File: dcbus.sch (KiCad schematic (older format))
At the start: 15 parts, among them K1 CONN_3, T1 COMMON MODE CHOKE

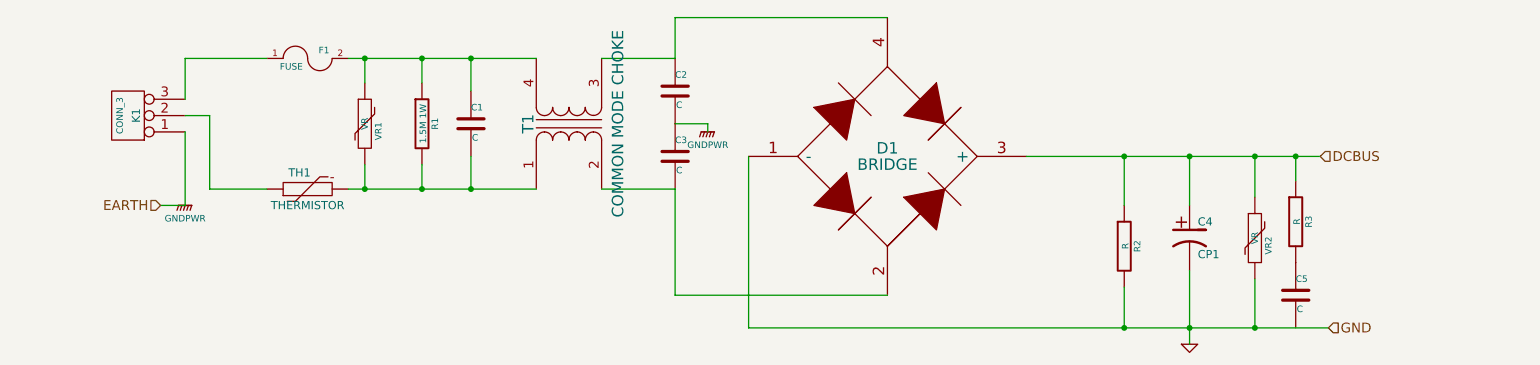
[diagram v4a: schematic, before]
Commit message: Add more protection, MOV to earth, MOV on dcbus
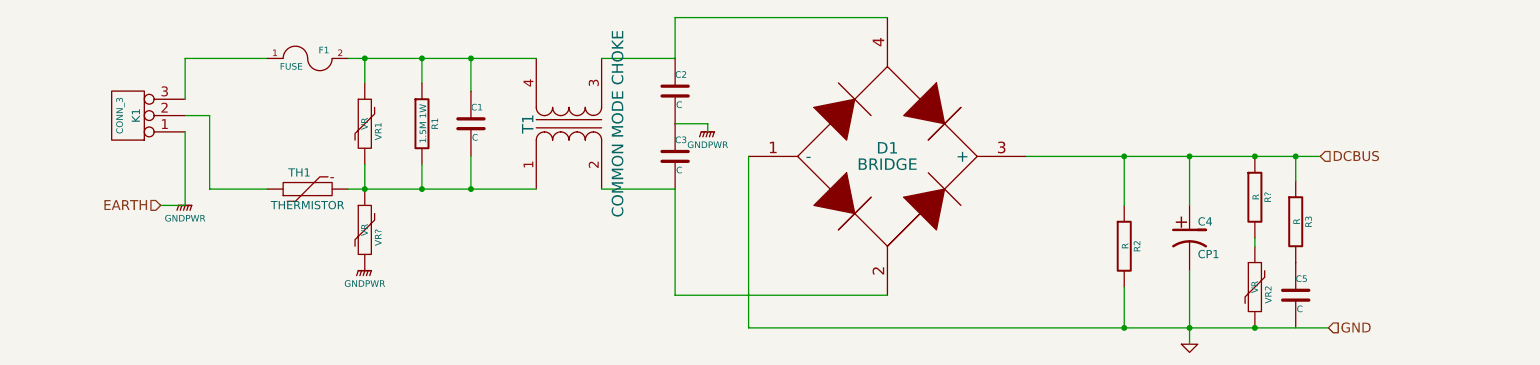
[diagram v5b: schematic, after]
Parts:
- added R?: R, symbol R
- added VR?: VR, symbol VR
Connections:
- net DCBUS: now also R?.1; no longer VR2.1
- net GNDPWR: now also VR?.2
- net at C1.2, R1.2, T1.1 (AA)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: now also VR?.1
- new net: R?.2, VR2.1
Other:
- moved on the sheet: VR2
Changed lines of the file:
@@
 L VR VR2
 U 1 1 537E750E
-P 9150 4050
-F 0 "VR2" V 9210 4004 40  0000 C TNN
-F 1 "VR" V 9150 4050 40  0000 C CNN
-F 2 "" H 9150 4050 60  0000 C CNN
-F 3 "" H 9150 4050 60  0000 C CNN
-	1    9150 4050
+P 9150 4350
+F 0 "VR2" V 9210 4304 40  0000 C TNN
+F 1 "VR" V 9150 4350 40  0000 C CNN
+F 2 "" H 9150 4350 60  0000 C CNN
+F 3 "" H 9150 4350 60  0000 C CNN
+	1    9150 4350
 	1    0    0    -1
 $EndComp
-Wire Wire Line
-	9150 3800 9150 3550
 Connection ~ 9150 3550
-Wire Wire Line
-	9150 4300 9150 4600
 Connection ~ 9150 4600
 $Comp
@@
 	8350 4350 8350 4600
 Connection ~ 8350 4600
+$Comp
+L R R?
+U 1 1 538051C9
+P 9150 3800
+F 0 "R?" V 9230 3800 40  0000 C CNN
+F 1 "R" V 9157 3801 40  0000 C CNN
+F 2 "" V 9080 3800 30  0000 C CNN
+F 3 "" H 9150 3800 30  0000 C CNN
+	1    9150 3800
+	1    0    0    -1
+$EndComp
+Wire Wire Line
+	9150 4050 9150 4100
+$Comp
+L VR VR?
+U 1 1 5381D2DF
+P 3700 4000
+F 0 "VR?" V 3760 3954 40  0000 C TNN
+F 1 "VR" V 3700 4000 40  0000 C CNN
+F 2 "" H 3700 4000 60  0000 C CNN
+F 3 "" H 3700 4000 60  0000 C CNN
+	1    3700 4000
+	1    0    0    -1
+$EndComp
+$Comp
+L GNDPWR #PWR?
+U 1 1 5381D36A
+P 3700 4250
+F 0 "#PWR?" H 3700 4300 40  0001 C CNN
+F 1 "GNDPWR" H 3700 4170 40  0000 C CNN
+F 2 "" H 3700 4250 60  0000 C CNN
+F 3 "" H 3700 4250 60  0000 C CNN
+	1    3700 4250
+	1    0    0    -1
+$EndComp
 $EndSCHEMATC

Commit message: begin working on output power stage
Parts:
- added C?: C, symbol C
- added R15, R16: R, symbol R
- gave numbers to parts that had none: 2
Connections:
- net GNDPWR: now also C?.2
- net at C1.2, R1.2, T1.1 (AA)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: now also C?.1
- new net DCBUSSENSE: R15.2, R16.1
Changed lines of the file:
@@
 $Descr A4 11693 8268
 encoding utf-8
-Sheet 2 3
+Sheet 2 5
 Title ""
 Date ""
@@
 	6050 3550 6050 4600
 Wire Wire Line
-	6050 4600 9600 4600
+	6050 4600 10050 4600
 Wire Wire Line
 	8750 4250 8750 4700
@@
 Connection ~ 3700 2950
 $Comp
-L GNDPWR #PWR2
+L GNDPWR #PWR3
 U 1 1 5377D78A
 P 5800 3400
-F 0 "#PWR2" H 5800 3450 40  0001 C CNN
+F 0 "#PWR3" H 5800 3450 40  0001 C CNN
 F 1 "GNDPWR" H 5800 3320 40  0000 C CNN
 F 2 "" H 5800 3400 60  0000 C CNN
@@
 	5600 4400 6900 4400
 $Comp
-L GND #PWR3
+L GND #PWR4
 U 1 1 5377D7C9
 P 8750 4700
-F 0 "#PWR3" H 8750 4700 30  0001 C CNN
+F 0 "#PWR4" H 8750 4700 30  0001 C CNN
 F 1 "GND" H 8750 4630 30  0001 C CNN
 F 2 "" H 8750 4700 60  0000 C CNN
@@
 Wire Wire Line
 	2750 3750 3100 3750
-Text HLabel 9550 3550 2    60   Input ~ 0
+Text HLabel 10000 3550 2    60   Input ~ 0
 DCBUS
 Wire Wire Line
-	7750 3550 9550 3550
-Text HLabel 9600 4600 2    60   Input ~ 0
+	7750 3550 10000 3550
+Text HLabel 10050 4600 2    60   Input ~ 0
 GND
-Text HLabel 2450 3850 0    60   Input ~ 0
+Text HLabel 2450 3700 0    60   Input ~ 0
 EARTH
-Wire Wire Line
-	2600 3850 2450 3850
 Wire Wire Line
 	8750 3550 8750 3850
@@
 Connection ~ 8350 4600
 $Comp
-L R R?
+L R R4
 U 1 1 538051C9
 P 9150 3800
-F 0 "R?" V 9230 3800 40  0000 C CNN
+F 0 "R4" V 9230 3800 40  0000 C CNN
 F 1 "R" V 9157 3801 40  0000 C CNN
 F 2 "" V 9080 3800 30  0000 C CNN
@@
 	9150 4050 9150 4100
 $Comp
-L VR VR?
+L VR VR3
 U 1 1 5381D2DF
 P 3700 4000
-F 0 "VR?" V 3760 3954 40  0000 C TNN
+F 0 "VR3" V 3760 3954 40  0000 C TNN
 F 1 "VR" V 3700 4000 40  0000 C CNN
 F 2 "" H 3700 4000 60  0000 C CNN
@@
 $EndComp
 $Comp
-L GNDPWR #PWR?
+L GNDPWR #PWR2
 U 1 1 5381D36A
-P 3700 4250
-F 0 "#PWR?" H 3700 4300 40  0001 C CNN
-F 1 "GNDPWR" H 3700 4170 40  0000 C CNN
-F 2 "" H 3700 4250 60  0000 C CNN
-F 3 "" H 3700 4250 60  0000 C CNN
-	1    3700 4250
-	1    0    0    -1
-$EndComp
+P 3850 4400
+F 0 "#PWR2" H 3850 4450 40  0001 C CNN
+F 1 "GNDPWR" H 3850 4320 40  0000 C CNN
+F 2 "" H 3850 4400 60  0000 C CNN
+F 3 "" H 3850 4400 60  0000 C CNN
+	1    3850 4400
+	1    0    0    -1
+$EndComp
+$Comp
+L R R15
+U 1 1 53899D3C
+P 9700 3800
+F 0 "R15" V 9780 3800 40  0000 C CNN
+F 1 "R" V 9707 3801 40  0000 C CNN
+F 2 "" V 9630 3800 30  0000 C CNN
+F 3 "" H 9700 3800 30  0000 C CNN
+	1    9700 3800
+	1    0    0    -1
+$EndComp
+$Comp
+L R R16
+U 1 1 53899D80
+P 9700 4350
+F 0 "R16" V 9780 4350 40  0000 C CNN
+F 1 "R" V 9707 4351 40  0000 C CNN
+F 2 "" V 9630 4350 30  0000 C CNN
+F 3 "" H 9700 4350 30  0000 C CNN
+	1    9700 4350
+	1    0    0    -1
+$EndComp
+Wire Wire Line
+	9700 4050 9700 4100
+Wire Wire Line
+	9700 4100 10000 4100
+Text HLabel 10000 4100 2    60   Input ~ 0
+DCBUSSENSE
+$Comp
+L C C?
+U 1 1 5389EB30
+P 4050 3950
+F 0 "C?" H 4050 4050 40  0000 L CNN
+F 1 "C" H 4056 3865 40  0000 L CNN
+F 2 "" H 4088 3800 30  0000 C CNN
+F 3 "" H 4050 3950 60  0000 C CNN
+	1    4050 3950
+	1    0    0    -1
+$EndComp
+Wire Wire Line
+	4050 4150 4050 4250
+Wire Wire Line
+	4050 4250 3700 4250
+Wire Wire Line
+	3850 4250 3850 4400
+Connection ~ 3850 4250
+Wire Wire Line
+	2450 3700 2600 3700
+Connection ~ 2600 3700
 $EndSCHEMATC

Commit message: populating boards
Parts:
- gave numbers to parts that had none: 1
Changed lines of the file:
@@
 DCBUSSENSE
 $Comp
-L C C?
+L C C21
 U 1 1 5389EB30
 P 4050 3950
-F 0 "C?" H 4050 4050 40  0000 L CNN
+F 0 "C21" H 4050 4050 40  0000 L CNN
 F 1 "C" H 4056 3865 40  0000 L CNN
 F 2 "" H 4088 3800 30  0000 C CNN
